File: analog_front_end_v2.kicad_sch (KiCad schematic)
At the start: 149 parts, among them J1 Conn_Coaxial, J3 Conn_01x01_Socket, J4 Conn_01x01_Socket, U1 ADL5531, U10 PMOD 2x6, U11 LP2985-5.0, U12 LP2985-5.0, U13 LT1363, U14 MAX 735, U15 LP2985-2.5, U16 MAX889SESA, U17 MAX6102, U2 ADL5531, U3 ADL5531, U4 PE4140B-Z, U5 ADF4360-9, U6 LTC1406, U7 THS4551, U8 LT1363, U9 PMOD 2x6

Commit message: Annotated all caps with voltage ratings
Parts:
- C30, C33: value 0.1uF -> 0.1u_10V
- C31: value 2.2uF -> 2.2uF_25V; MOC TMK107ABJ225KA-T -> TMK107ABJ225KA-T
- C32: value 2.2uF -> 2.2uF_25V
- C34, C36, C38, C40, C41, C49, C51: value 10uF -> 10u_16V
- C35: value 56pF -> 56p_50V
- C37: value 2.2nF -> 2.2n_50V
- C39: value 150pF -> 150p_150V
- C48: value 47uF -> 47u_16V
- C55, C56: value 4.7uF -> 4.7u_16V
- C57: value 1uF -> 1u_16V
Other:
- moved on the sheet: C32, C36, C38, C40, C41, C58, C59, C60, R25, R26, R27, R28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

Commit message: Update notes/decisions in schematics/pcb for clarity
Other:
- note added: "Note: L6 and L7 value sets the PLL centre output frequency 250nH should get the 88MHz to 100MHz range roughly"
- note added: "Note: Using 7-12V alligator clip compatible jack for benchtop power supplies (Regs support up to 16V)"
- note added: "PCB: To reduce mutual coupling, the inductors should be placed at right angles to one another."
- note removed: "L6 and L7 value sets the PLL centre output frequency 250nH should get the 88MHz to 100MHz range roughly"
- note removed: "To reduce mutual coupling, the inductors should be placed at right angles to one another."
- note removed: "Use 7-12V alligator clip compatible jack for benchtop power supplies (Regs support up to 16V)"
- moved on the sheet: R15, R23, R24, R40, TP10, TP12, TP16, TP20, TP21

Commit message: Begin adding tolerance information to passives
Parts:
- removed TP11, TP9: TestPoint, TestPoint:TestPoint_Pad_D1.0mm, symbol Connector:TestPoint
- removed TP5: ~, TestPoint:TestPoint_Pad_D1.0mm, symbol Connector:TestPoint
- C1, C2, C3, C4, C5, C6, C7, C8: Tolerance (none) -> 1%
- C12, C14, C18: Tolerance (none) -> 5%
- C13, C17: value 1n_50V -> 1n_50V_5%
- R36: value 100k -> 100k_1%
- R37: value 66.5k -> 66.5k_1%
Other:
- note added: "2nd order LC passive RF Band Pass Filter"
- note added: "Goals: 1. 50 ohm impedance 2. Minimize parasitics (inc trace resistance) as much as possible in layout to lock on center freq 3. Via stiching to ground around RF traces 4. Short traces with minimal direction changes"
- note removed: "2nd order passive RF Band Pass Filter"
- note removed: "Goals: 1. 50 ohm impedance 2. Minimize parasitics as much as possible in layout to lock on center freq 3. Via stiching to ground around RF traces 4. Short traces with minimal direction changes"
- moved on the sheet: C1, C10, C11, C12, C14, C15, C16, C18, C19, C2, C20, C3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

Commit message: Annotate tolerance of all caps in sch
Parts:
- C10, C11, C15, C16, C19, C20, C28, C29, C43, C46, C52, C57, C58, C59, C9: Tolerance (none) -> 5%
- C13, C17: value 1n_50V_5% -> 1n_50V; Tolerance (none) -> 5%
- C27, C35, C37, C39, C50: Tolerance (none) -> 1%
- C30, C31, C32, C33, C34, C36, C38, C40, C41, C42, C44, C45, C47, C48, C49, C51, C53, C54, C55, C56, C60: Tolerance (none) -> 10%

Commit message: Annotate resistor tolerances on the schematic
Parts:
- R1, R10, R11, R15, R16, R17, R18, R19, R2, R20, R21, R23, R24, R26, R28, R29, R3, R31, R32, R35, R38, R39, R40, R41, R42, R43, R44, R45, R46: Tolerance (none) -> 1%
- R12: Tolerance (none) -> 5%
- R36: value 100k_1% -> 100k; Tolerance (none) -> 1%
- R37: value 66.5k_1% -> 66.5k; Tolerance (none) -> 1%

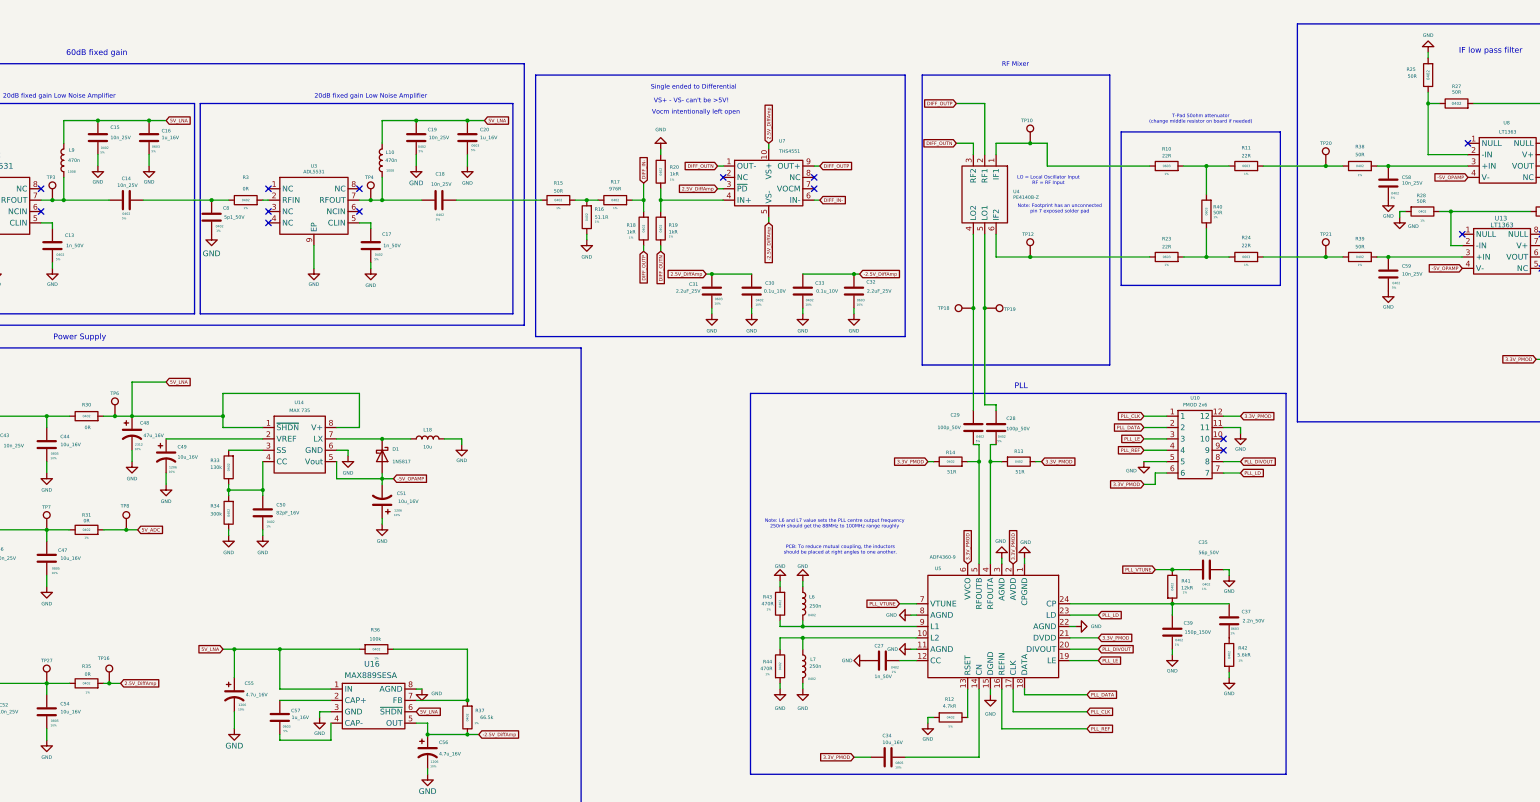
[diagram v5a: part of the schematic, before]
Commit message: Annotate tolerance values for missed resistors
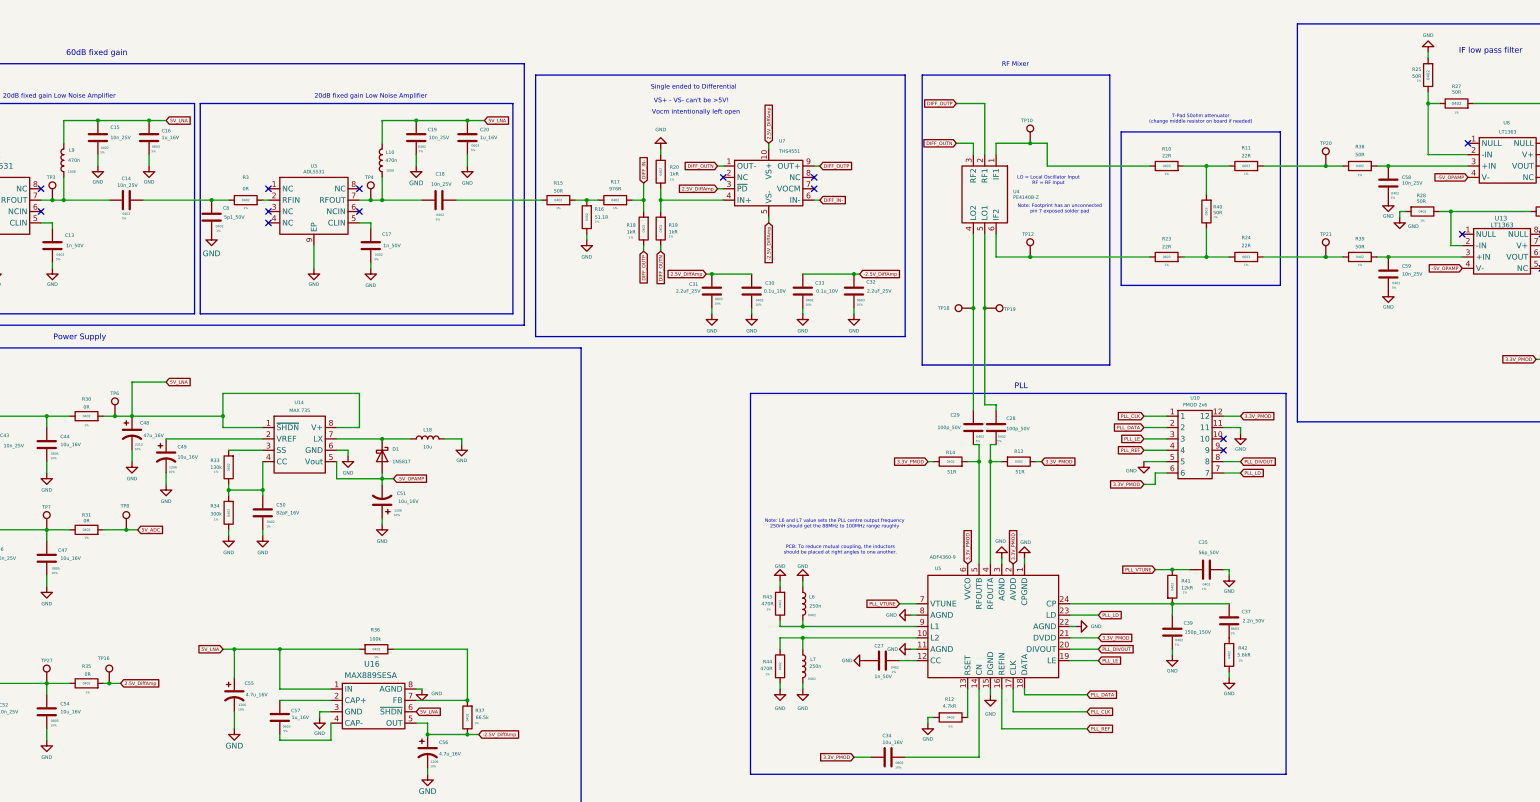
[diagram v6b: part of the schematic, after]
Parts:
- R25, R27, R30, R33, R34: Tolerance (none) -> 1%
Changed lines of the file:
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@@
 		)
 		(property "Tolerance" "1%"
-			(at 276.86 164.592 90)
+			(at 276.86 164.338 90)
 			(effects
 				(font
@@
 		)
 		(property "Value" "66.5k"
-			(at 301.498 177.8 0)
+			(at 300.482 177.8 0)
 			(effects
 				(font
@@
 			)
 		)
+		(property "Tolerance" "1%"
+			(at 241.046 122.936 0)
+			(effects
+				(font
+					(size 0.4572 0.4572)
+				)
+			)
+		)
 		(pin "2"
 		)
@@
 		(dnp no)
 		(property "Reference" "R30"
-			(at 212.09 107.95 90)
+			(at 212.09 106.68 90)
 			(effects
 				(font
@@
 		)
 		(property "Value" "0R"
-			(at 212.344 113.03 90)
+			(at 212.09 108.458 90)
 			(effects
 				(font
@@
 			)
 		)
+		(property "Tolerance" "1%"
+			(at 212.09 112.522 90)
+			(effects
+				(font
+					(size 0.4572 0.4572)
+				)
+			)
+		)
 		(pin "2"
 		)
@@
 			)
 		)
+		(property "Tolerance" "1%"
+			(at 518.16 42.672 90)
+			(effects
+				(font
+					(size 0.4572 0.4572)
+				)
+			)
+		)
 		(pin "2"
 		)
@@
 		(dnp no)
 		(property "Reference" "R25"
-			(at 508 33.02 0)
+			(at 509.27 33.02 0)
 			(effects
 				(font
@@
 		)
 		(property "Value" "50R"
-			(at 508.254 34.544 0)
+			(at 509.27 34.544 0)
 			(effects
 				(font
@@
 			)
 		)
+		(property "Tolerance" "1%"
+			(at 509.778 35.56 0)
+			(effects
+				(font
+					(size 0.4572 0.4572)
+				)
+			)
+		)
 		(pin "2"
 		)
@@
 			)
 		)
+		(property "Tolerance" "1%"
+			(at 241.046 133.604 0)
+			(effects
+				(font
+					(size 0.4572 0.4572)
+				)
+			)
+		)

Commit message: Begin adding I/Q component handling
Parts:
- removed C30, C33: 0.1u_10V, Capacitor_SMD:C_0402_1005Metric, symbol Device:C
- removed C31, C32: 2.2uF_25V, Capacitor_SMD:C_0603_1608Metric, symbol Device:C
- removed R1, R2, R3: 0R, Resistor_SMD:R_0402_1005Metric, symbol Device:R
- removed R15: 50R, Resistor_SMD:R_0402_1005Metric, symbol Device:R
- removed R16: 51.1R, Resistor_SMD:R_0402_1005Metric, symbol Device:R
- removed R17: 976R, Resistor_SMD:R_0402_1005Metric, symbol Device:R
- removed R18, R19, R20: 1kR, Resistor_SMD:R_0402_1005Metric, symbol Device:R
- removed TP1, TP10, TP12, TP18, TP19, TP2, TP20, TP21, TP3, TP4: TestPoint, TestPoint:TestPoint_Pad_D1.0mm, symbol Connector:TestPoint
- removed TP16, TP27, TP6, TP7, TP8: ~, TestPoint:TestPoint_Pad_D1.0mm, symbol Connector:TestPoint
- removed U7: THS4551, TheEEView_Footprint_Lib:THS4551, symbol TheEEView_Global_Lib:THS4551
- added L11, L13: 159n, Inductor_SMD:L_1008_2520Metric, symbol Device:L
- added L12: 470n, Inductor_SMD:L_1008_2520Metric, symbol Device:L
- added U18, U19, U20, U21: PAT1220-C-0DB, RF_Converter:RF_Attenuator_Susumu_PAT1220, symbol RF:PAT1220-C-0DB
- added U7: ~, symbol TheEEView_Global_Lib:LT5546EUF
- C1, C5, L1, L5: now not fitted
- C6: value 5p1_50V -> 220pF; MOC GCM1555C1H5R1FA16D -> (none); Size 0402 -> (none); Tolerance 1% -> (none)
- C7: value 5p1_50V -> 15.9pF; MOC GCM1555C1H5R1FA16D -> (none); Size 0402 -> (none); Tolerance 1% -> (none)
- C8: value 5p1_50V -> 15.9pF; MOC GCM1555C1H5R1FA16D -> (none); Tolerance 1% -> (none)
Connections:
- net GND: now also C8.1, L12.2, L13.1, L13.2, U18.3, U19.3, U20.3, U21.3, U7.1 (GND), U7.3 (IF-), U7.4 (GND); no longer C6.2, C8.2
- net at C7.1: now also C6.2, L11.1, L12.1; no longer C12.2
- net at U2.2 (RFIN): now also U19.2
- net at C5.1, L4.2, L5.1: now also U18.1; no longer C6.1
- net at U1.2 (RFIN): now also U18.2
- net at C14.2: now also U20.1; no longer C8.1
- net at C18.2: now also U21.1
- net at U3.2 (RFIN): now also U20.2
- new net: C12.2, U19.1
- new net: C8.2, L11.2, U7.2 (IF+)
- new net: C6.1, U21.2
- no-connect marks 30 -> 27
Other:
- note added: "3x20dB fixed gain amps (60dB fixed gain)"
- note added: "TODO: Finish I/Q component creation"
- note added: "TODO: Select caps and inductors and indicate tolerance values"
- note removed: "20dB fixed gain Low Noise Amplifier"
- note removed: "60dB fixed gain"
- note removed: "Single ended to Differential"
- note removed: "VS+ - VS- can't be >5V!"
- note removed: "Vocm intentionally left open"
- moved on the sheet: C10, C11, C12, C14, C15, C16, C18, C19, C20, C9, L10, L8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

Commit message: Hooked up VCC, VCTRL and IFDET pins of the LT5546EUF
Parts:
- added C21: 10u_50V, Capacitor_SMD:C_1206_3216Metric, symbol Device:C
- added C22: 10n_25V, Capacitor_SMD:C_0402_1005Metric, symbol Device:C
- added C23: 10u_16V, Capacitor_SMD:C_0805_2012Metric, symbol Device:C
- added C24: 1u_16V, Capacitor_SMD:C_0603_1608Metric, symbol Device:C
- added C25, C26: 1n_50V, Capacitor_SMD:C_0402_1005Metric, symbol Device:C
- added C30: 1p5F, Capacitor_SMD:C_0402_1005Metric, symbol Device:C
- added C31: 1p8F, Capacitor_SMD:C_0402_1005Metric, symbol Device:C
- added R1: 0R, Resistor_SMD:R_0402_1005Metric, symbol Device:R
- added R2: 100R, Resistor_SMD:R_0402_1005Metric, symbol Device:R
- added U22: LP2985-3.3, Package_TO_SOT_SMD:SOT-23-5, symbol Regulator_Linear:LP2985-3.3
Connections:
- net GND: now also C21.1, C22.1, C23.1, C24.1, C25.2, C26.2, C30.1, C31.1, U22.2 (GND)
- net VIN: now also C21.2, U22.1 (VIN), U22.3 (ON/~{OFF})
- net DEMOD_Q-: now reaches U7.13 (QOUT-)
- net DEMOD_Q+: now reaches U7.14 (QOUT+)
- net DEMOD_I-: now reaches U7.15 (IOUT-)
- net DEMOD_I+: now reaches U7.16 (IOUT+)
- net 3.3V: now reaches U7.5 (VCC)
- net 3.3V: now also U7.8 (VCC), C24.2, C25.1, C26.1, R1.2
- net at U7.6 (VCTRL): now also C30.2, R2.2
- net DEMOD_IF_DET: now reaches U7.7 (IFDET)
- net DEMOD_IF_DET: now also C31.2
- new net: C22.2, U22.4 (BP)
- new net: C23.2, R1.1, U22.5 (VOUT)
- new net DEMOD_VCTRL: R2.1
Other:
- moved on the sheet: C1, C10, C11, C12, C13, C14, C15, C16, C17, C18, C19, C2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
